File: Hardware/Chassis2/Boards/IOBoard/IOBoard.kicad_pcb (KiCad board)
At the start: 6 copper layers, 260 x 45 mm, 31 parts, among them IC10 DRDNB21D-7, J1 UJ2-B-HR-G-V, J10 Conn_02x03_Counter_Clockwise, J11 Conn_02x03_Counter_Clockwise, J12 Conn_02x08_Counter_Clockwise, J13 Conn_02x03_Counter_Clockwise, J14 Conn_02x10_Counter_Clockwise, J6 776231-1, J7 Conn_02x08_Counter_Clockwise, K1 AWHSH105D00G, K2 AWHSH105D00G, U6 BTS462TATMA1

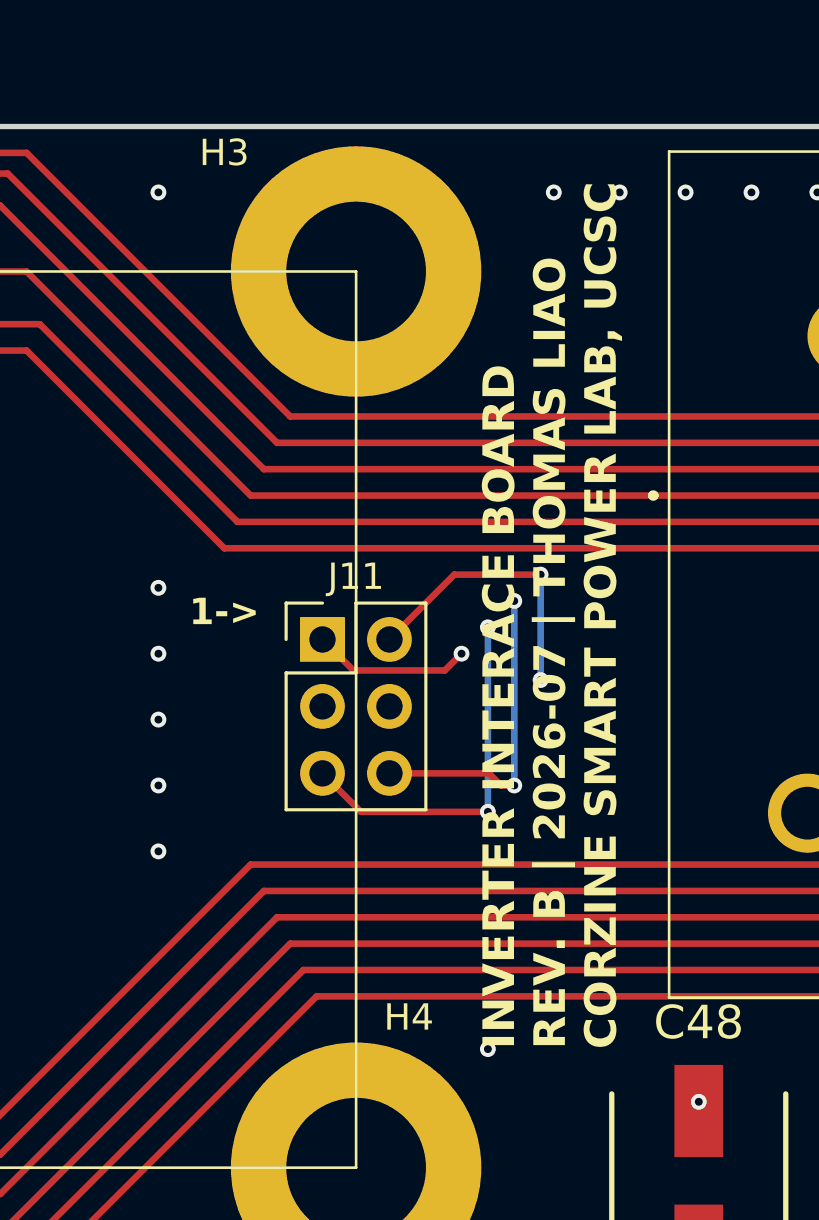
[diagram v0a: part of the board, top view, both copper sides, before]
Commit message: Update IO Board silkscreen, ExM pinout
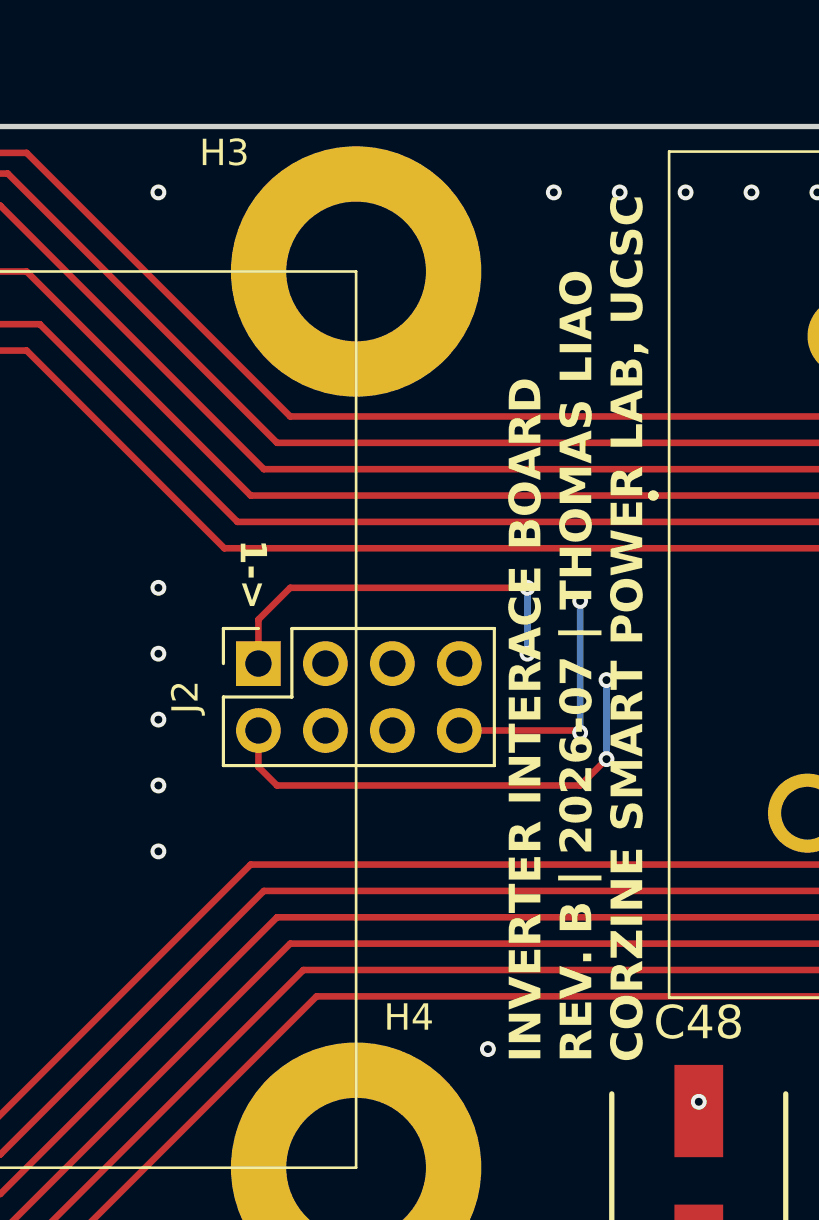
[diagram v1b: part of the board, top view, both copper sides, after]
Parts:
- removed J11: Conn_02x03_Counter_Clockwise, Connector_PinHeader_2.54mm:PinHeader_2x03_P2.54mm_Vertical
- added J2: Conn_02x04_Counter_Clockwise, Connector_PinSocket_2.54mm:PinSocket_2x04_P2.54mm_Vertical, F.Cu at (81.3, 20.4)
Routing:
- net /FAULT: track 96.8 -> 84.6 mm, vias 4 -> 2
- net /MD_FIBER_TX: track 86.7 -> 93.1 mm, vias 3 -> 4
- net /MD_FIBER_RX: track 90.6 -> 95.7 mm
- net /MD_FIBER_SYNC: track 98.8 -> 93.9 mm

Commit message: Finalize IO Board Connectors, Standoffs, PartNum
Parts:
- H1, H2, H3, H4, H5, H6, H7, H8: value MountingHole -> 971250581; footprint MountingHole:MountingHole_5.3mm_M5_ISO7380_Pad -> InverterCom:971250581
- J10, J13: value Conn_02x03_Counter_Clockwise -> TSW-103-18-G-D; footprint Connector_PinHeader_2.54mm:PinHeader_2x03_P2.54mm_Vertical -> InverterCom:TSW-103-18-G-D
- J12, J7: value Conn_02x08_Counter_Clockwise -> TSW-108-18-F-D; footprint Connector_PinHeader_2.54mm:PinHeader_2x08_P2.54mm_Vertical -> InverterCom:TSW-108-18-F-D
- J14: value Conn_02x10_Counter_Clockwise -> TSW-110-18-T-D; footprint Connector_PinSocket_2.54mm:PinSocket_2x10_P2.54mm_Vertical -> InverterCom:TSW-110-18-T-D
- J2: value Conn_02x04_Counter_Clockwise -> SSW-104-01-L-D; footprint Connector_PinSocket_2.54mm:PinSocket_2x04_P2.54mm_Vertical -> InverterCom:SSW-104-01-L-D
- moved J6 3.25 mm to (113.3, 18.0)
- moved U6 1.00 mm to (125.0, 41.0)
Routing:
- net /CAN1_GND: track 64.5 -> 74.4 mm
- net /+12V_A: track 16.6 -> 24.0 mm
- net /CAN1_HIGH: track 67.2 -> 74.6 mm
- net /CAN1_JUMPER_B: track 78.0 -> 85.4 mm
- net /DOUT4_A: track 75.2 -> 78.5 mm, vias 4 -> 5
- net /GND_A: track 24.0 -> 26.5 mm, vias 100 -> 99
- net /+12V_SWITCHED_A: track 19.5 -> 17.3 mm
- net /CAN2_+5V: track 82.3 -> 80.3 mm
- net /CAN2_LOW: track 72.3 -> 70.3 mm
- net /CAN2_JUMPER_A: track 89.1 -> 87.1 mm
- net /CAN2_HIGH: track 74.1 -> 72.1 mm
- net /CAN1_LOW: track 63.6 -> 65.5 mm
- net /THROTTLE1_IN_A: track 79.7 -> 77.8 mm
- net /O_PRECHARGE_DC_LINK_+_Z: track 109.2 -> 110.5 mm
- net /I_+VIN_Z: track 21.4 -> 22.8 mm
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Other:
- board text added: "INVERTER IO BOARD REV. B | 2026-07 | THOMAS LIAO CORZINE SMART POWER LAB, UCSC"
- board text added: "P/N: HW-C2-PCB-IO-A"
- board text removed: "INVERTER INTERACE BOARD REV. B | 2026-07 | THOMAS LIAO CORZINE SMART POWER LAB, UCSC"
